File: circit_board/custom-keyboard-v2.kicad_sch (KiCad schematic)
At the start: 141 parts, among them J1 i2c_display, J2 Adafruit-AP3602A-PCB, SW1 SW_Push, SW10 SW_Push, SW11 SW_Push, SW12 SW_Push, SW13 SW_Push, SW14 SW_Push, SW15 SW_Push, SW16 SW_Push, SW17 SW_Push, SW18 SW_Push, SW19 SW_Push, SW2 SW_Push, SW20 SW_Push, SW21 SW_Push, SW22 SW_Push, SW23 SW_Push, SW24 SW_Push, SW25 SW_Push, SW26 SW_Push, SW27 SW_Push, SW28 SW_Push, SW29 SW_Push, SW3 SW_Push, SW30 SW_Push, SW31 SW_Push, SW32 SW_Push, SW33 SW_Push, SW34 SW_Push, SW35 SW_Push, SW36 SW_Push, SW37 SW_Push, SW38 SW_Push, SW39 SW_Push, SW4 SW_Push, SW40 SW_Push, SW41 SW_Push, SW42 SW_Push, SW43 SW_Push, SW44 SW_Push, SW45 SW_Push, SW46 SW_Push, SW5 SW_Push, SW6 SW_Push, SW7 SW_Push, SW8 SW_Push, SW9 SW_Push

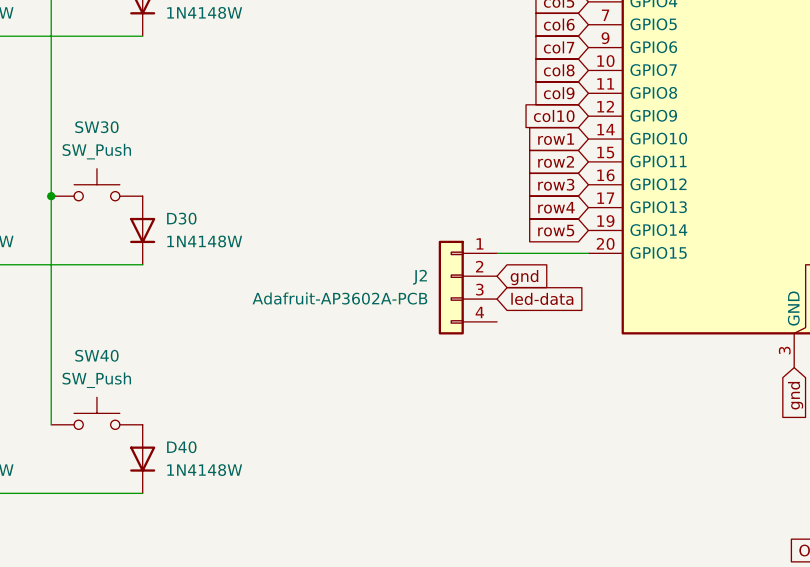
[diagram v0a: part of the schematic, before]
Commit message: Removed 3.3V to 5V converter from the LED input
This turned out to be unnecessary after getting the circit board printed
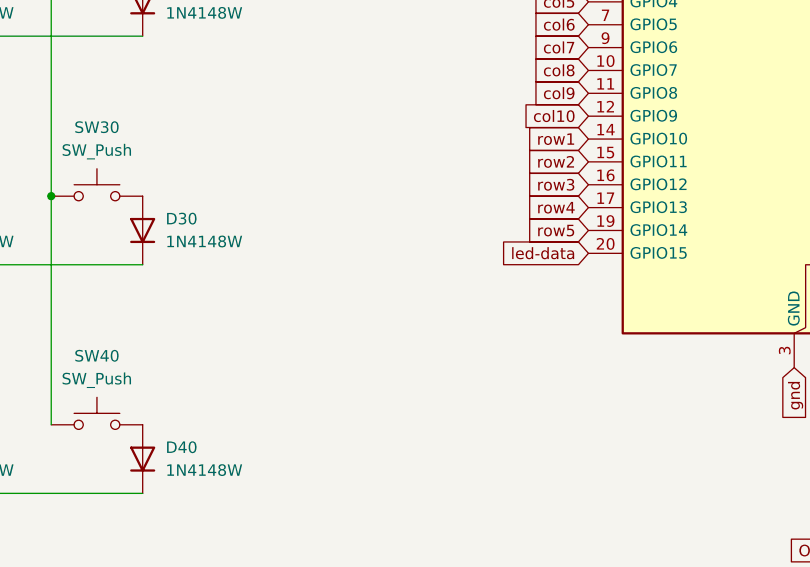
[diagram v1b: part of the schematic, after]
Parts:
- removed J2: Adafruit-AP3602A-PCB, Connector_PinHeader_2.54mm:PinHeader_1x04_P2.54mm_Vertical, symbol Connector_Generic:Conn_01x04
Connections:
- net led-data: now also A1.20 (GPIO15)
